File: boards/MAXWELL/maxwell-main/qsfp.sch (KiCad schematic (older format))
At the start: 17 parts, among them J29 CONN_QSFP_HOST, J30 QSFP_CAGE, U2 XC7K160T-2FFG676C

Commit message: Continued schematic review. Added footprints for C1-C282.
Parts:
- C271, C273, C274, C275: footprint (none) -> azonenberg_pcb:EIA_1210_CAP_NOSILK
- C272, C276, C277, C278, C279, C280: footprint (none) -> azonenberg_pcb:EIA_0402_CAP_NOSILK
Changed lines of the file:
@@
 F 0 "C280" V 8400 1400 50  0000 C CNN
 F 1 "0.1 uF" V 8500 1450 50  0000 C CNN
-F 2 "" H 8488 1100 50  0001 C CNN
+F 2 "azonenberg_pcb:EIA_0402_CAP_NOSILK" H 8488 1100 50  0001 C CNN
 F 3 "" H 8450 1250 50  0001 C CNN
 	1    8450 1250
@@
 F 0 "C279" V 8400 1200 50  0000 C CNN
 F 1 "0.1 uF" V 8500 1250 50  0000 C CNN
-F 2 "" H 8488 900 50  0001 C CNN
+F 2 "azonenberg_pcb:EIA_0402_CAP_NOSILK" H 8488 900 50  0001 C CNN
 F 3 "" H 8450 1050 50  0001 C CNN
 	1    8450 1050
@@
 F 0 "C271" H 1365 5146 50  0000 L CNN
 F 1 "22 uF" H 1365 5055 50  0000 L CNN
-F 2 "" H 1288 4950 50  0001 C CNN
+F 2 "azonenberg_pcb:EIA_1210_CAP_NOSILK" H 1288 4950 50  0001 C CNN
 F 3 "" H 1250 5100 50  0001 C CNN
 	1    1250 5100
@@
 F 0 "C272" H 1815 5146 50  0000 L CNN
 F 1 "0.1 uF" H 1815 5055 50  0000 L CNN
-F 2 "" H 1738 4950 50  0001 C CNN
+F 2 "azonenberg_pcb:EIA_0402_CAP_NOSILK" H 1738 4950 50  0001 C CNN
 F 3 "" H 1700 5100 50  0001 C CNN
 	1    1700 5100
@@
 F 0 "L4" V 1392 5500 40  0000 C CNN
 F 1 "1 uH" V 1468 5500 40  0000 C CNN
-F 2 "" H 1550 5500 60  0000 C CNN
+F 2 "" H 1550 5500 60  0001 C CNN
 F 3 "" H 1550 5500 60  0000 C CNN
 	1    1550 5500
@@
 F 0 "C273" H 1965 5696 50  0000 L CNN
 F 1 "22 uF" H 1965 5605 50  0000 L CNN
-F 2 "" H 1888 5500 50  0001 C CNN
+F 2 "azonenberg_pcb:EIA_1210_CAP_NOSILK" H 1888 5500 50  0001 C CNN
 F 3 "" H 1850 5650 50  0001 C CNN
 	1    1850 5650
@@
 F 0 "C276" H 2465 5696 50  0000 L CNN
 F 1 "0.1 uF" H 2465 5605 50  0000 L CNN
-F 2 "" H 2388 5500 50  0001 C CNN
+F 2 "azonenberg_pcb:EIA_0402_CAP_NOSILK" H 2388 5500 50  0001 C CNN
 F 3 "" H 2350 5650 50  0001 C CNN
 	1    2350 5650
@@
 F 0 "L5" V 1392 6050 40  0000 C CNN
 F 1 "1 uH" V 1468 6050 40  0000 C CNN
-F 2 "" H 1550 6050 60  0000 C CNN
+F 2 "" H 1550 6050 60  0001 C CNN
 F 3 "" H 1550 6050 60  0000 C CNN
 	1    1550 6050
@@
 F 0 "C274" H 1965 6246 50  0000 L CNN
 F 1 "22 uF" H 1965 6155 50  0000 L CNN
-F 2 "" H 1888 6050 50  0001 C CNN
+F 2 "azonenberg_pcb:EIA_1210_CAP_NOSILK" H 1888 6050 50  0001 C CNN
 F 3 "" H 1850 6200 50  0001 C CNN
 	1    1850 6200
@@
 F 0 "C277" H 2465 6246 50  0000 L CNN
 F 1 "0.1 uF" H 2465 6155 50  0000 L CNN
-F 2 "" H 2388 6050 50  0001 C CNN
+F 2 "azonenberg_pcb:EIA_0402_CAP_NOSILK" H 2388 6050 50  0001 C CNN
 F 3 "" H 2350 6200 50  0001 C CNN
 	1    2350 6200
@@
 F 0 "L6" V 1392 6600 40  0000 C CNN
 F 1 "1 uH" V 1468 6600 40  0000 C CNN
-F 2 "" H 1550 6600 60  0000 C CNN
+F 2 "" H 1550 6600 60  0001 C CNN
 F 3 "" H 1550 6600 60  0000 C CNN
 	1    1550 6600
@@
 F 0 "C275" H 1965 6796 50  0000 L CNN
 F 1 "22 uF" H 1965 6705 50  0000 L CNN
-F 2 "" H 1888 6600 50  0001 C CNN
+F 2 "azonenberg_pcb:EIA_1210_CAP_NOSILK" H 1888 6600 50  0001 C CNN
 F 3 "" H 1850 6750 50  0001 C CNN
 	1    1850 6750
@@
 F 0 "C278" H 2465 6796 50  0000 L CNN
 F 1 "0.1 uF" H 2465 6705 50  0000 L CNN
-F 2 "" H 2388 6600 50  0001 C CNN
+F 2 "azonenberg_pcb:EIA_0402_CAP_NOSILK" H 2388 6600 50  0001 C CNN
 F 3 "" H 2350 6750 50  0001 C CNN
 	1    2350 6750

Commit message: Continued assigning footprints. Done with everything up to and not including resistors.
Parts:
- J29: footprint (none) -> azonenberg_pcb:CONN_QSFP+_TE_2110819-1
- J30: footprint (none) -> azonenberg_pcb:CONN_QSFP_CAGE_TE_2110487-1
- L4, L5, L6: footprint (none) -> azonenberg_pcb:EIA_0805_INDUCTOR_NOSILK
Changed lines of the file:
@@
 F 0 "J30" H 4530 992 50  0000 L CNN
 F 1 "QSFP_CAGE" H 4530 901 50  0000 L CNN
-F 2 "" H 4450 950 50  0001 C CNN
+F 2 "azonenberg_pcb:CONN_QSFP_CAGE_TE_2110487-1" H 4450 950 50  0001 C CNN
 F 3 "~" H 4450 950 50  0001 C CNN
 	1    4450 950
@@
 F 0 "J29" H 4800 7325 50  0000 C CNN
 F 1 "CONN_QSFP_HOST" H 4800 7234 50  0000 C CNN
-F 2 "" H 4400 4350 50  0001 L CNN
+F 2 "azonenberg_pcb:CONN_QSFP+_TE_2110819-1" H 4400 4350 50  0001 L CNN
 F 3 "" H 4400 4350 50  0001 C CNN
 	1    4400 4350
@@
 F 0 "L4" V 1392 5500 40  0000 C CNN
 F 1 "1 uH" V 1468 5500 40  0000 C CNN
-F 2 "" H 1550 5500 60  0001 C CNN
+F 2 "azonenberg_pcb:EIA_0805_INDUCTOR_NOSILK" H 1550 5500 60  0001 C CNN
 F 3 "" H 1550 5500 60  0000 C CNN
 	1    1550 5500
@@
 F 0 "L5" V 1392 6050 40  0000 C CNN
 F 1 "1 uH" V 1468 6050 40  0000 C CNN
-F 2 "" H 1550 6050 60  0001 C CNN
+F 2 "azonenberg_pcb:EIA_0805_INDUCTOR_NOSILK" H 1550 6050 60  0001 C CNN
 F 3 "" H 1550 6050 60  0000 C CNN
 	1    1550 6050
@@
 F 0 "L6" V 1392 6600 40  0000 C CNN
 F 1 "1 uH" V 1468 6600 40  0000 C CNN
-F 2 "" H 1550 6600 60  0001 C CNN
+F 2 "azonenberg_pcb:EIA_0805_INDUCTOR_NOSILK" H 1550 6600 60  0001 C CNN
 F 3 "" H 1550 6600 60  0000 C CNN
 	1    1550 6600

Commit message: Assigned footprints for all resistors
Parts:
- R120: footprint (none) -> azonenberg_pcb:EIA_0402_RES_NOSILK
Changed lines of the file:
@@
 Sheet 13 18
 Title "MAXWELL Main Board"
-Date "2020-06-22"
+Date "2020-06-23"
 Rev "0.1"
 Comp "Antikernel Labs"
@@
 F 0 "R120" V 8850 800 50  0000 C CNN
 F 1 "100" V 8950 800 50  0000 C CNN
-F 2 "" V 8880 800 50  0001 C CNN
+F 2 "azonenberg_pcb:EIA_0402_RES_NOSILK" V 8880 800 50  0001 C CNN
 F 3 "" H 8950 800 50  0001 C CNN
 	1    8950 800

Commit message: Began assigning IC footprints
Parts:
- U2: footprint (none) -> azonenberg_pcb:BGA_676_27x27_FULLARRAY_1MM_FFG676
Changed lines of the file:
@@
 F 0 "U2" H 9600 3900 50  0000 L CNN
 F 1 "XC7K160T-2FFG676C" H 9600 3800 50  0000 L CNN
-F 2 "" H 9600 3950 50  0001 C CNN
+F 2 "azonenberg_pcb:BGA_676_27x27_FULLARRAY_1MM_FFG676" H 9600 3950 50  0001 C CNN
 F 3 "" H 9600 3950 50  0001 C CNN
 	12   9600 3950

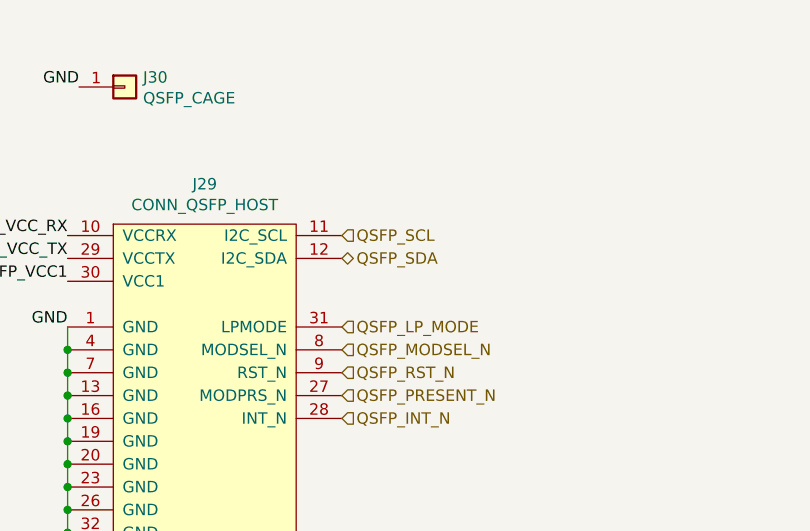
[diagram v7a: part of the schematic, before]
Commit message: Renamed I2C buses to be consistent
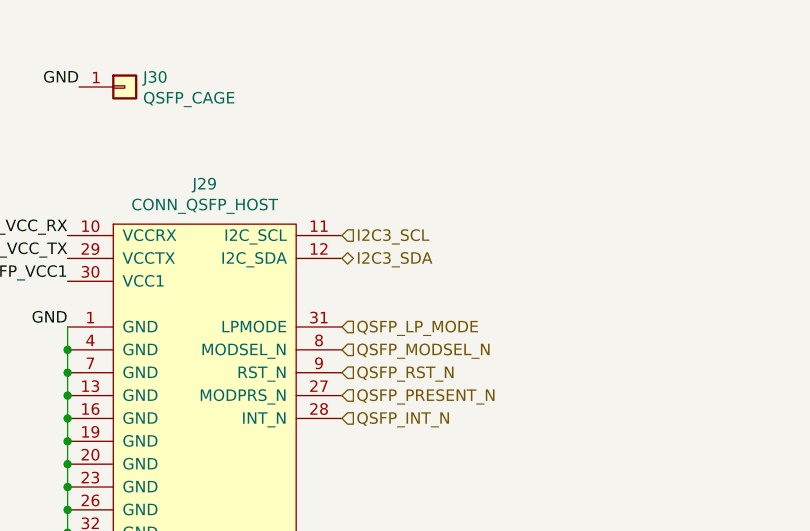
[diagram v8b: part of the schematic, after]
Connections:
- net QSFP_SCL renamed I2C3_SCL
- net QSFP_SDA renamed I2C3_SDA
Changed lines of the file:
@@
 	4200 3000 4200 3100
 Text HLabel 5400 1700 2    50   BiDi ~ 0
-QSFP_SDA
+I2C3_SDA
 Text HLabel 5400 1600 2    50   Input ~ 0
-QSFP_SCL
+I2C3_SCL
 Text Label 5400 3300 0    50   ~ 0
 QSFP_RX1_P
